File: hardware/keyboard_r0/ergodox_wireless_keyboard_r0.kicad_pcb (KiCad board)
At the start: 2 copper layers, 180.1 x 154.6 mm, 184 parts

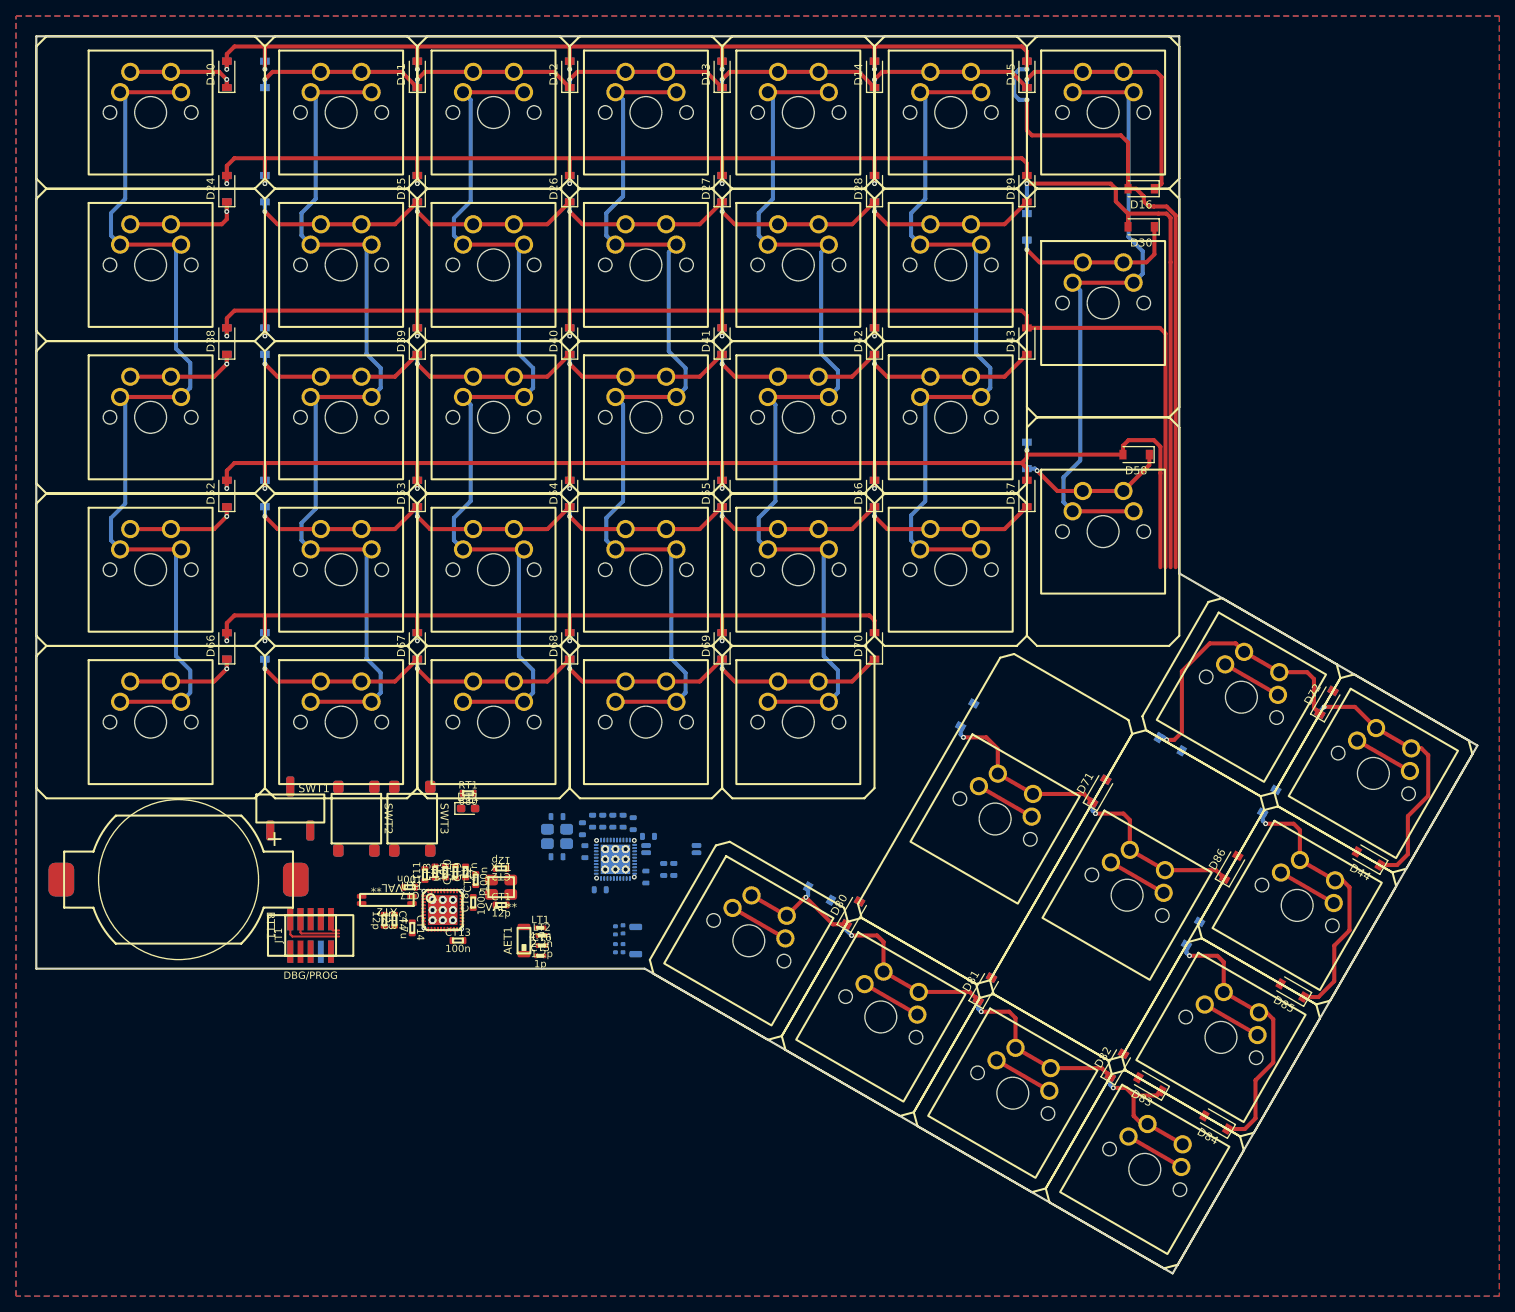
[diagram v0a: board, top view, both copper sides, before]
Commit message: Update PCB to KiCAD 8.0.
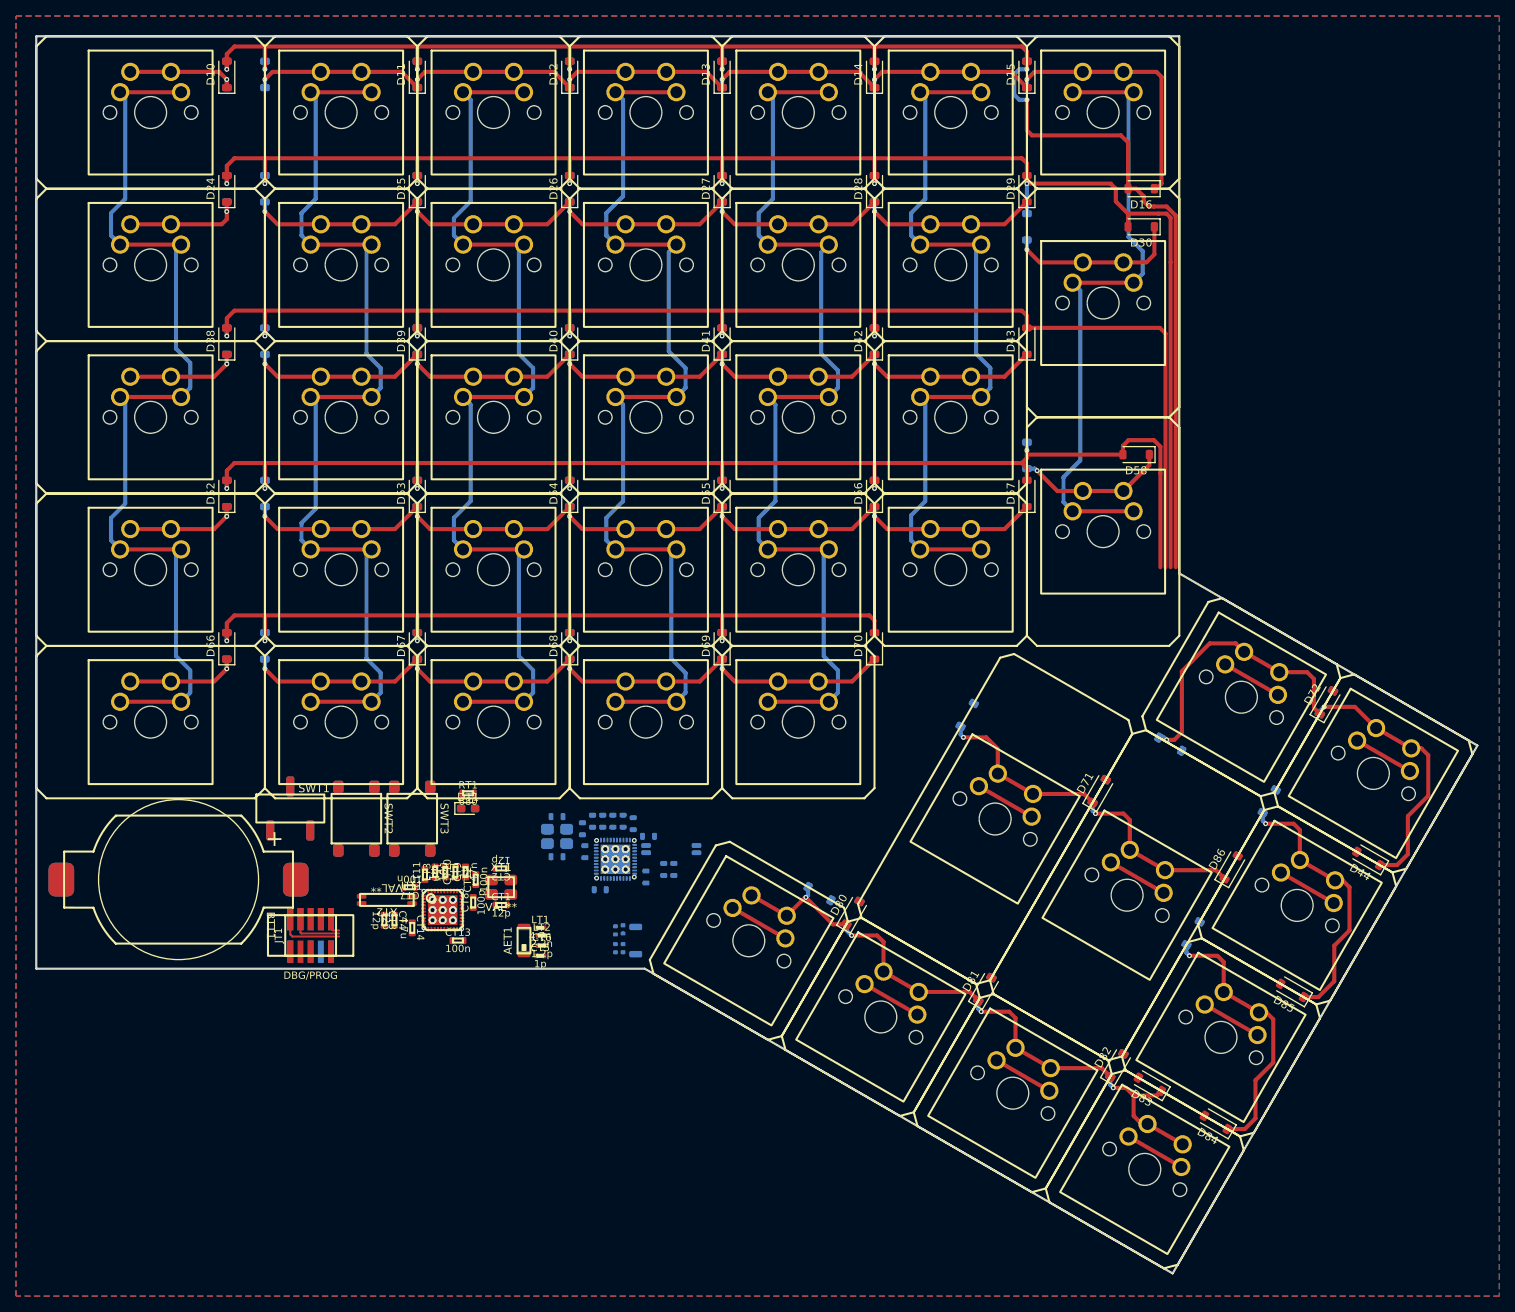
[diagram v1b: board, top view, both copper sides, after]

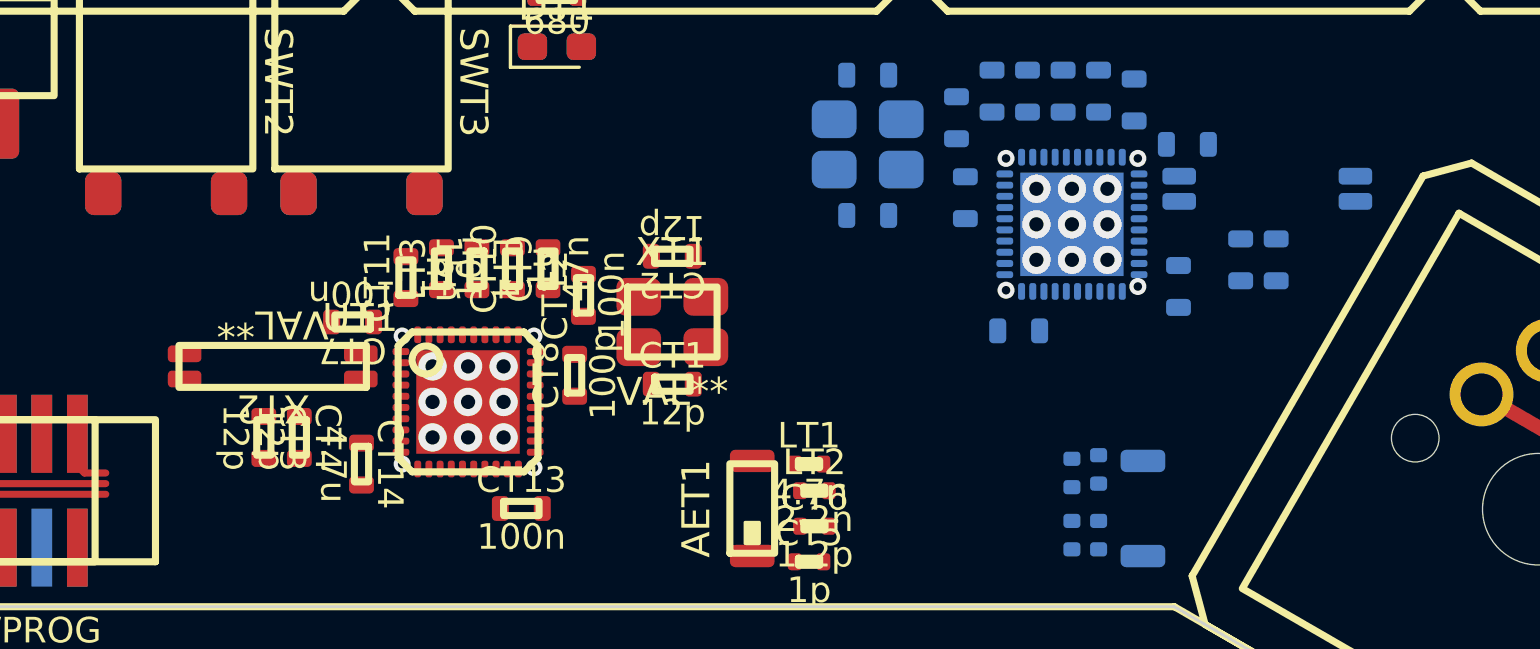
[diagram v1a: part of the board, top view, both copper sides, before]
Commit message: Remove optional low-frequency oscillator circuit.
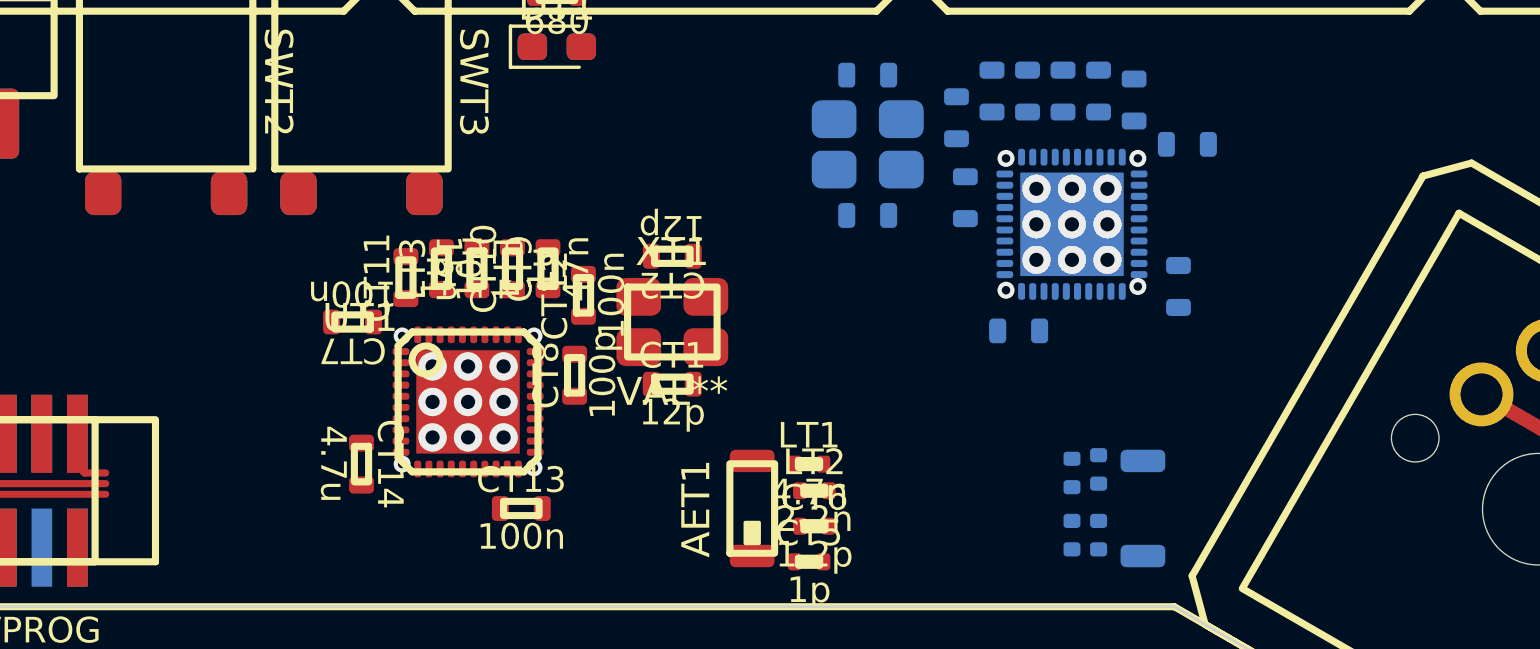
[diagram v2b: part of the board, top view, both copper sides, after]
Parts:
- removed CB3, CB4, CT3, CT4: 12p, mass:0603
- removed XB2, XT2: 32.768k, mass:MC-146
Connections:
- UB1 pad 14: /Bottom Microcontroller/COL1 -> /Bottom Microcontroller/COL3
- UB1 pad 15: /Bottom Microcontroller/COL2 -> /Bottom Microcontroller/COL4
- UB1 pad 17: /Bottom Microcontroller/COL5 -> unconnected-(UB1-P0.20-Pad17)
- UB1 pad 2: Net-(UB1-P0.00/XL1) -> /Bottom Microcontroller/ROW0
- UB1 pad 22: /Bottom Microcontroller/COL3 -> /Bottom Microcontroller/COL5
- UB1 pad 23: /Bottom Microcontroller/COL4 -> /Bottom Microcontroller/COL6
- UB1 pad 3: Net-(UB1-P0.01/XL2) -> /Bottom Microcontroller/ROW1
- UB1 pad 31: /Bottom Microcontroller/COL0 -> /Bottom Microcontroller/COL2
- UB1 pad 34: /Bottom Microcontroller/COL6 -> unconnected-(UB1-P0.28-Pad34)
- UB1 pad 35: /Bottom Microcontroller/ROW1 -> /Bottom Microcontroller/ROW3
- UB1 pad 36: /Bottom Microcontroller/ROW0 -> /Bottom Microcontroller/ROW2
- UB1 pad 4: /Bottom Microcontroller/ROW2 -> /Bottom Microcontroller/ROW4
- UB1 pad 5: /Bottom Microcontroller/ROW3 -> /Bottom Microcontroller/ROW5
- UB1 pad 6: /Bottom Microcontroller/ROW4 -> /Bottom Microcontroller/COL0
- UB1 pad 7: /Bottom Microcontroller/ROW5 -> /Bottom Microcontroller/COL1
- UT1 pad 14: /Bottom Microcontroller/COL1 -> /Bottom Microcontroller/COL3
- UT1 pad 15: /Bottom Microcontroller/COL2 -> /Bottom Microcontroller/COL4
- UT1 pad 17: /Bottom Microcontroller/COL5 -> unconnected-(UT1-P0.20-Pad17)
- UT1 pad 2: Net-(UT1-P0.00/XL1) -> /Bottom Microcontroller/ROW0
- UT1 pad 22: /Bottom Microcontroller/COL3 -> /Bottom Microcontroller/COL5
- UT1 pad 23: /Bottom Microcontroller/COL4 -> /Bottom Microcontroller/COL6
- UT1 pad 3: Net-(UT1-P0.01/XL2) -> /Bottom Microcontroller/ROW1
- UT1 pad 31: /Bottom Microcontroller/COL0 -> /Bottom Microcontroller/COL2
- UT1 pad 34: /Bottom Microcontroller/COL6 -> unconnected-(UT1-P0.28-Pad34)
- UT1 pad 35: /Bottom Microcontroller/ROW1 -> /Bottom Microcontroller/ROW3
- UT1 pad 36: /Bottom Microcontroller/ROW0 -> /Bottom Microcontroller/ROW2
- UT1 pad 4: /Bottom Microcontroller/ROW2 -> /Bottom Microcontroller/ROW4
- UT1 pad 5: /Bottom Microcontroller/ROW3 -> /Bottom Microcontroller/ROW5
- UT1 pad 6: /Bottom Microcontroller/ROW4 -> /Bottom Microcontroller/COL0
- UT1 pad 7: /Bottom Microcontroller/ROW5 -> /Bottom Microcontroller/COL1
